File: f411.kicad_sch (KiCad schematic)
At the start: 19 parts, among them J9 Conn_02x04_Top_Bottom, SW1 SW_Push, SW2 SW_Push, U2 STM32F411CEU6

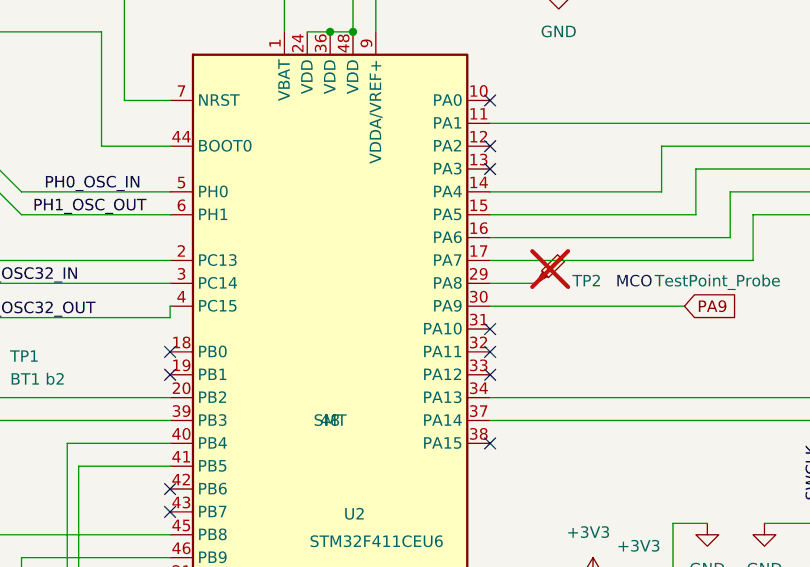
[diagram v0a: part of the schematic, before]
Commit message: 3v3 trace moved to back side.
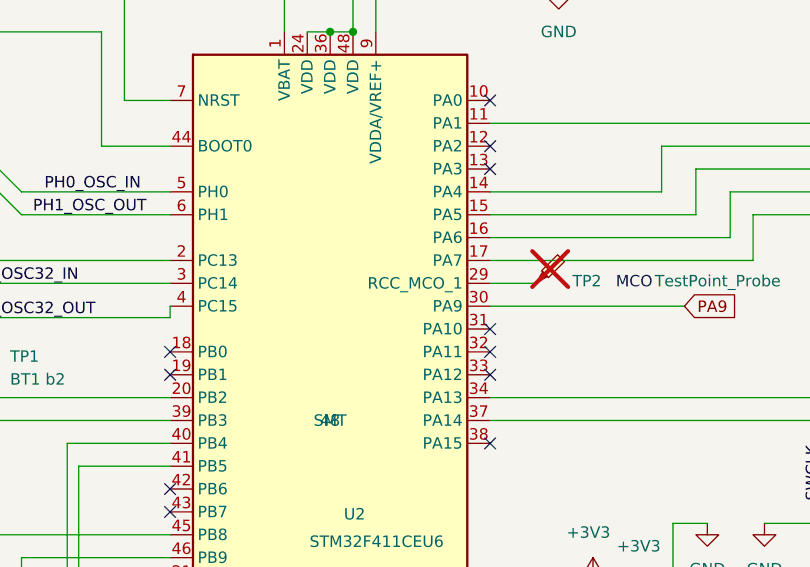
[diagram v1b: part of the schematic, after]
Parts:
- J9: MfgPart HC-PM254-5.0H-2x8PS -> HC-PM254-5.0H-2x4PS-02A
- U2: footprint Package_DFN_QFN:QFN-48-1EP_7x7mm_P0.5mm_EP5.6x5.6mm -> ProjectLib:QFN-48-1EP_7x7mm_P0.5mm_EP5.6x5.6mm
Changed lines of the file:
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@@
 			)
 		)
-		(property "MfgPart" "HC-PM254-5.0H-2x8PS"
+		(property "MfgPart" "HC-PM254-5.0H-2x4PS-02A"
 			(at 190.5 125.73 0)
 			(effects
@@
 			)
 		)
-		(property "Footprint" "Package_DFN_QFN:QFN-48-1EP_7x7mm_P0.5mm_EP5.6x5.6mm"
+		(property "Footprint" "ProjectLib:QFN-48-1EP_7x7mm_P0.5mm_EP5.6x5.6mm"
 			(at 129.54 140.97 0)
 			(effects
@@
 		)
 		(pin "29"
+			(alternate "RCC_MCO_1")
 		)
 		(pin "4"

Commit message: MCU moved down closer to radio. Connectors need better arrangement.
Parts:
- TP2: now left out of the parts list
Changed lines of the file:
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@@
 		(unit 1)
 		(exclude_from_sim no)
-		(in_bom yes)
+		(in_bom no)
 		(on_board yes)
 		(dnp yes)

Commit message: ongoing
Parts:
- TP2: value TestPoint_Probe -> MCO
- U2: footprint ProjectLib:QFN-48-1EP_7x7mm_P0.5mm_EP5.6x5.6mm -> Package_DFN_QFN:QFN-48-1EP_7x7mm_P0.5mm_EP5.6x5.6mm
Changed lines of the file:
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@@
 			)
 		)
-		(property "Value" "TestPoint_Probe"
+		(property "Value" "MCO"
 			(at 180.848 87.376 0)
 			(effects
@@
 			)
 		)
-		(property "Description" "test point (alternative probe-style design)"
+		(property "Description" "test point"
 			(at 167.64 87.63 0)
 			(effects
@@
 			)
 		)
-		(property "Footprint" "ProjectLib:QFN-48-1EP_7x7mm_P0.5mm_EP5.6x5.6mm"
+		(property "Footprint" "Package_DFN_QFN:QFN-48-1EP_7x7mm_P0.5mm_EP5.6x5.6mm"
 			(at 129.54 140.97 0)
 			(effects

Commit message: reduced with of board.
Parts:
- U2: footprint Package_DFN_QFN:QFN-48-1EP_7x7mm_P0.5mm_EP5.6x5.6mm -> ProjectLib:QFN-48-1EP_7x7mm_P0.5mm_EP5.6x5.6mm
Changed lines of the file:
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@@
 			)
 		)
-		(property "Footprint" "Package_DFN_QFN:QFN-48-1EP_7x7mm_P0.5mm_EP5.6x5.6mm"
+		(property "Footprint" "ProjectLib:QFN-48-1EP_7x7mm_P0.5mm_EP5.6x5.6mm"
 			(at 129.54 140.97 0)
 			(effects

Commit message: ongoing
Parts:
- removed TP1: BT1 b2, ProjectLib:TestPoint_Pad_D1.0mm, symbol ProjectLib:TestPoint
- removed TP2: MCO, ProjectLib:TestPoint_Pad_D1.0mm, symbol ProjectLib:TestPoint_Probe
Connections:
- net +3V3: no longer J9.a2 (Pin_a2), J9.b4 (Pin_b4)
- net GND: no longer J9.a1 (Pin_a1), J9.b1 (Pin_b1)
- net SCL1: no longer J9.a3 (Pin_a3)
- net SDA1: no longer J9.a4 (Pin_a4)
- net SWCLK: no longer J9.b2 (Pin_b2)
- net SWDIO: no longer J9.b3 (Pin_b3)
- net PA8-MCO: now reaches U2.29 (PA8)
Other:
- note removed: "MCO"
- moved on the sheet: R10, R9

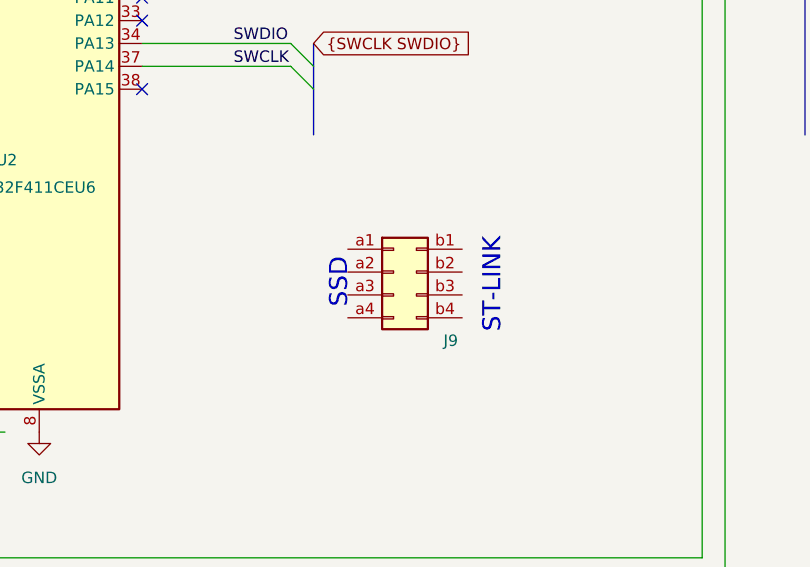
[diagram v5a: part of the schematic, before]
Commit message: settled on 24-pins. Fairly clean castillated pin header but no footprint yet. Decided against rotating radio.
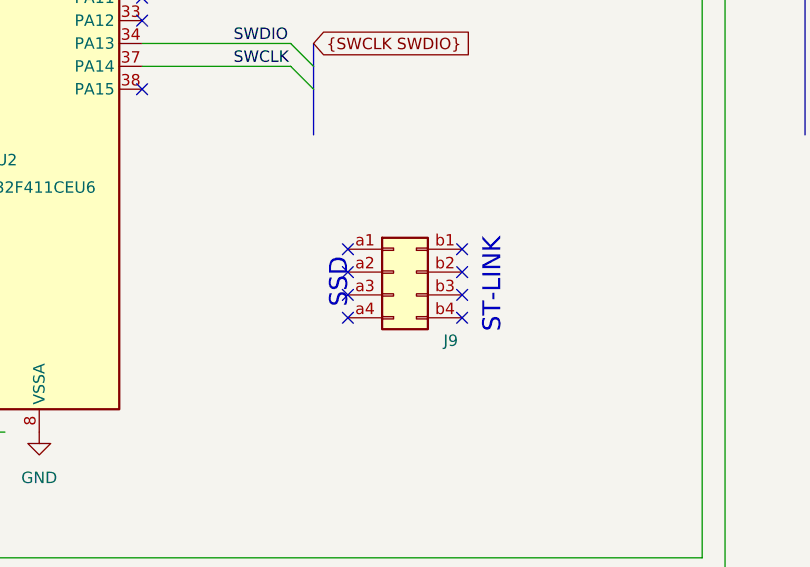
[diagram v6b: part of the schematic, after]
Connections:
- no-connect marks 15 -> 23
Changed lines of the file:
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@@
+	)
+	(no_connect
+		(at 185.42 130.81)
 	)
 	(no_connect
 		(at 127 110.49)
+	)
+	(no_connect
+		(at 185.42 128.27)
+	)
+	(no_connect
+		(at 185.42 125.73)
+	)
+	(no_connect
+		(at 198.12 130.81)
 	)
 	(no_connect
@@
 	(no_connect
 		(at 162.56 92.71)
+	)
+	(no_connect
+		(at 185.42 123.19)
+	)
+	(no_connect
+		(at 198.12 128.27)
 	)
 	(no_connect
@@
 	)
 	(no_connect
+		(at 198.12 123.19)
+	)
+	(no_connect
 		(at 127 130.81)
 	)
@@
 	)
 	(no_connect
+		(at 198.12 125.73)
+	)
+	(no_connect

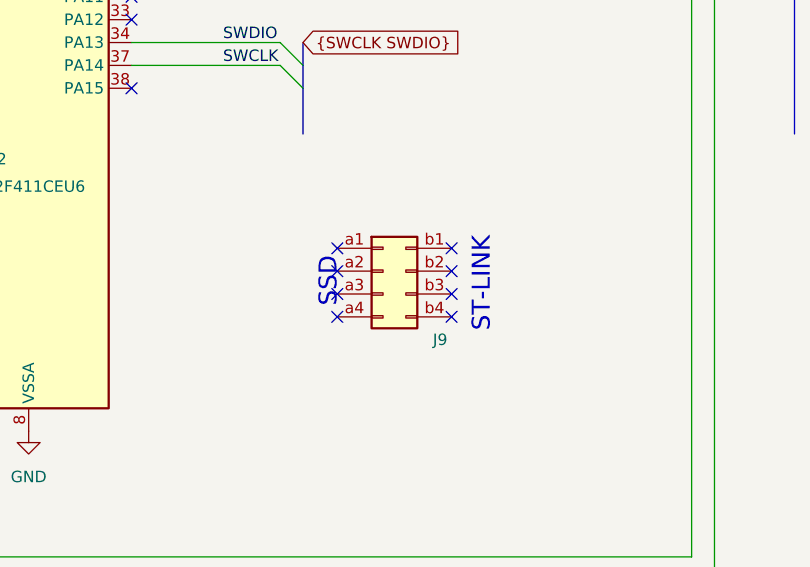
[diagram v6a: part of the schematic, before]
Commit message: added footprint and step model. Cleaned up silkscreen and fab layers.
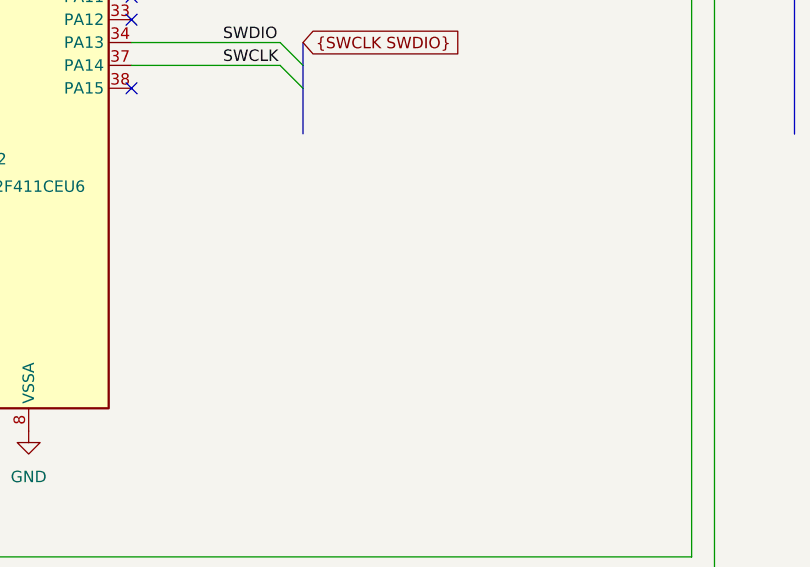
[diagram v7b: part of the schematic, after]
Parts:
- removed J9: Conn_02x04_Top_Bottom, ProjectLib:PinSocket_2x04_P2.54mm_Vertical_SMD, symbol ProjectLib:Conn_02x04_Row_Letter_First
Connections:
- no-connect marks 23 -> 15
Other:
- note removed: "SSD"
- note removed: "ST-LINK"
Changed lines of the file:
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@@
 		(rev "v0.1.0")
-	)
-	(text "SSD"
-		(exclude_from_sim no)
-		(at 184.404 127 90)
-		(effects
-			(font
-				(size 2 2)
-			)
-		)
-	)
-	(text "ST-LINK"
-		(exclude_from_sim no)
-		(at 201.422 127.254 90)
-		(effects
-			(font
-				(size 2 2)
-			)
-		)
 	)
 	(junction
@@
 	)
 	(no_connect
-		(at 185.42 130.81)
-	)
-	(no_connect
 		(at 127 110.49)
-	)
-	(no_connect
-		(at 185.42 128.27)
-	)
-	(no_connect
-		(at 185.42 125.73)
-	)
-	(no_connect
-		(at 198.12 130.81)
 	)
 	(no_connect
@@
 	)
 	(no_connect
-		(at 185.42 123.19)
-	)
-	(no_connect
-		(at 198.12 128.27)
-	)
-	(no_connect
 		(at 127 113.03)
 	)
@@
 	)
 	(no_connect
-		(at 198.12 123.19)
-	)
-	(no_connect
 		(at 127 130.81)
 	)
@@
 	(no_connect
 		(at 127 123.19)
-	)
-	(no_connect
-		(at 198.12 125.73)
 	)
 	(no_connect
@@
 					(unit 1)
 				)
-			)
-		)
-	)
-	(symbol
-		(lib_id "ProjectLib:Conn_02x04_Row_Letter_First")
-		(at 190.5 125.73 0)
-		(unit 1)
-		(exclude_from_sim no)
-		(in_bom yes)
-		(on_board yes)
-		(dnp no)
-		(property "Reference" "J9"
-			(at 196.85 133.35 0)
-			(effects
-				(font
-					(size 1.27 1.27)
-				)
-			)
-		)
-		(property "Value" "Conn_02x04_Top_Bottom"
-			(at 201.168 122.682 90)
-			(effects
-				(font
-					(size 1.27 1.27)
-				)
-				(hide yes)
-			)
-		)
-		(property "Footprint" "ProjectLib:PinSocket_2x04_P2.54mm_Vertical_SMD"
-			(at 190.5 125.73 0)
-			(effects
-				(font
-					(size 1.27 1.27)
-				)
-				(hide yes)
-			)
-		)
-		(property "Datasheet" "~"
-			(at 190.5 125.73 0)
-			(effects
-				(font
-					(size 1.27 1.27)
-				)
-				(hide yes)
-			)
-		)
-		(property "Description" "Generic connector, double row, 02x04, row letter first pin numbering scheme (pin number consists of a letter for the row and a number for the pin index in this row. a1, ..., aN; b1, ..., bN), script generated (kicad-library-utils/schlib/autogen/connector/)"
-			(at 190.5 125.73 0)
-			(effects
-				(font
-					(size 1.27 1.27)
-				)
-				(hide yes)
-			)
-		)
-		(property "Manufacturer" "Hong Cheng"
-			(at 190.5 125.73 0)
-			(effects
-				(font
-					(size 1.27 1.27)
-				)
-				(hide yes)
-			)
-		)
-		(property "MfgPart" "HC-PM254-5.0H-2x4PS-02A"
-			(at 190.5 125.73 0)
-			(effects
-				(font
-					(size 1.27 1.27)
-				)
-				(hide yes)
-			)
-		)
-		(property "Note" ""
-			(at 190.5 125.73 0)
-			(effects
-				(font
-					(size 1.27 1.27)
-				)
-				(hide yes)
-			)
-		)
-		(property "Notes" "or equivalent"
-			(at 190.5 125.73 0)
-			(effects
-				(font
-					(size 1.27 1.27)
-				)
-				(hide yes)
-			)
-		)
-		(property "MountType" "SMT"
-			(at 190.5 125.73 0)
-			(effects
-				(font
-					(size 1.27 1.27)
-				)
-				(hide yes)
-			)
-		)
-		(property "Package" "2x04_P2.54mm, verticle pinsocket"
-			(at 190.5 125.73 0)
-			(effects
-				(font
-					(size 1.27 1.27)
-				)
-				(hide yes)
-			)
-		)
-		(pin "a1"
-		)
-		(pin "b4"
-		)
-		(pin "a4"
-		)
-		(pin "b3"
-		)
-		(pin "b1"
-		)
-		(pin "b2"
-		)
-		(pin "a2"
-		)
-		(pin "a3"
-		)
-		(instances
-			(project "LoRa-stm411"
-				(path "/0c2d0c14-8850-4a30-bb78-b2f40cb442ba/f12d0b95-be3f-41e2-8b41-943aec5e1edf"
-					(reference "J9")
-					(unit 1)
-				)
